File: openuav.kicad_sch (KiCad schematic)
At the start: 35 parts, among them J1 Conn_01x06, J31 Conn_01x09, J32 Conn_01x09, J33 Conn_01x09, J99 USB_C_Receptacle_USB2.0, U1 STM32G431CBUx, U3 LSM6DSR, U4 LPS22HH, U5 TPS54202DDC, U6 W25N01GVZEIG, U7 XC6206P332MR

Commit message: new PCB WIP
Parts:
- removed J1: Conn_01x06, Connector_PinHeader_2.54mm:PinHeader_2x03_P2.54mm_Vertical, symbol Connector_Generic:Conn_01x06
- removed J31, J32, J33: Conn_01x09, Connector_PinHeader_2.54mm:PinHeader_1x09_P2.54mm_Vertical, symbol Connector_Generic:Conn_01x09
- added C14: 1u, Capacitor_SMD:C_0402_1005Metric, symbol Device:C_Small
- added J1, J10, J11, J12, J13, J14, J15, J16, J17, J18, J19, J2, J20, J21, J22, J23, J24, J25, J26, J27, J28, J29, J3, J30, J31, J32, J4, J5, J6, J7, J8, J9: Conn_01x01, TestPoint:TestPoint_THTPad_1.5x1.5mm_Drill0.7mm, symbol Connector_Generic:Conn_01x01
- added R5: 68k, Resistor_SMD:R_0402_1005Metric, symbol Device:R_Small
- added R6: 10k, Resistor_SMD:R_0402_1005Metric, symbol Device:R_Small
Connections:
- net +3V3: now also J29.1 (Pin_1)
- net +5V: now also J10.1 (Pin_1), J14.1 (Pin_1), J18.1 (Pin_1), J2.1 (Pin_1), J6.1 (Pin_1)
- net +BATT: now also R5.1
- net BOOT0: now also J28.1 (Pin_1)
- net GND: now also C14.2, J1.1 (Pin_1), J13.1 (Pin_1), J17.1 (Pin_1), J21.1 (Pin_1), J27.1 (Pin_1), J5.1 (Pin_1), J9.1 (Pin_1), R6.2
- net I2C_CLK: now also U1.31 (PA9), J20.1 (Pin_1); no longer U1.16 (PC4)
- net I2C_SDA: now also U1.30 (PA8), J19.1 (Pin_1); no longer U1.5 (PF0)
- net NRST: now also J31.1 (Pin_1)
- net PWM_1: now also J22.1 (Pin_1)
- net PWM_2: now also J23.1 (Pin_1)
- net PWM_3: now also J24.1 (Pin_1)
- net PWM_4: now also J25.1 (Pin_1)
- net SPI1_CS: now also U1.18 (PB1); no longer U1.19 (PB2)
- net SPI3_CS: now also U1.44 (PB6); no longer U1.47 (PB9)
- net SPI3_MISO: now also U1.42 (PB4); no longer U1.40 (PC11)
- net SWCLK: now also J30.1 (Pin_1)
- net SWDIO: now also J32.1 (Pin_1)
- net UART_1_RX: now also J3.1 (Pin_1)
- net UART_1_TX: now also U1.16 (PC4), J4.1 (Pin_1); no longer U1.31 (PA9)
- net UART_2_RX: now also U1.38 (PA15), J7.1 (Pin_1); no longer U1.42 (PB4)
- net UART_2_TX: now also J8.1 (Pin_1)
- net UART_3_RX: now also U1.40 (PC11), J11.1 (Pin_1); no longer U1.24 (PB11)
- net UART_3_TX: now also U1.47 (PB9), J12.1 (Pin_1); no longer U1.22 (PB10)
- net CURRENT: now reaches U1.6 (PF1)
- net CURRENT: now also J26.1 (Pin_1)
- new net UART_4_RX: J15.1 (Pin_1), U1.22 (PB10)
- new net UART_4_TX: J16.1 (Pin_1), U1.24 (PB11)
- new net VOLTAGE: C14.1, R5.2, R6.1, U1.5 (PF0)
- no-connect marks 12 -> 11
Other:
- moved on the sheet: H1, H2, H3, H4

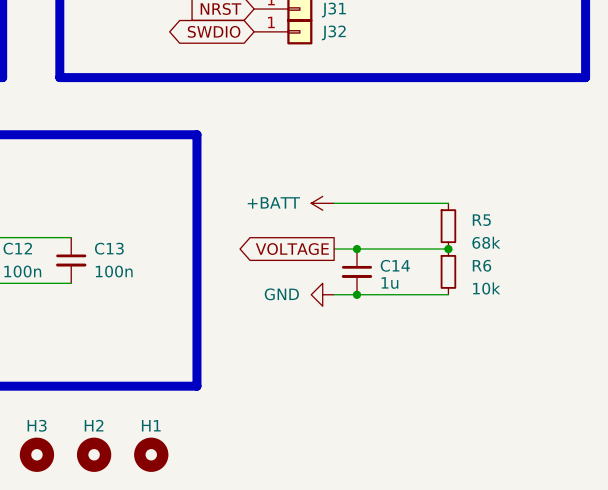
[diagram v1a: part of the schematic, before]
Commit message: Finish draft PCB design
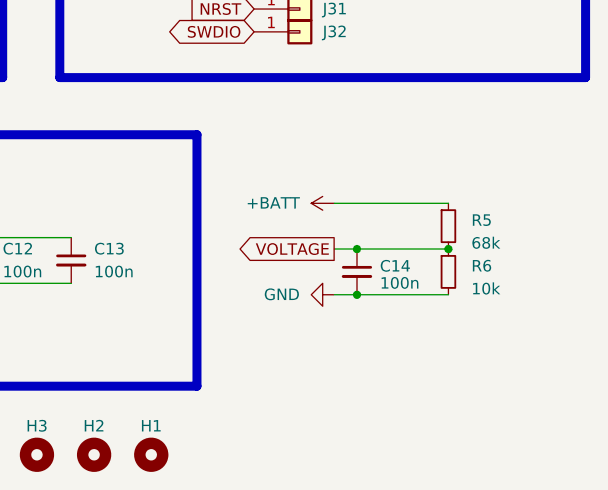
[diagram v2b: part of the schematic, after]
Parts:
- C14: value 1u -> 100n; LCSC (none) -> C307331
- C15: LCSC (none) -> C19702
- J99: footprint Connector_USB:USB_C_Receptacle_GCT_USB4105-xx-A_16P_TopMnt_Horizontal -> Connector_Custom_Pads:TYPE-C-31-M-12; LCSC (none) -> C2894897
- R1, R2: LCSC (none) -> C25905
- R3: LCSC (none) -> C25741
- R4: LCSC (none) -> C852522
- R5: LCSC (none) -> C36871
- R6: LCSC (none) -> C17414
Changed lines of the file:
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@@
+      (effects (font (size 1.27 1.27)) hide)
+    )
+    (property "LCSC" "C17414" (at 266.7 172.72 0)
       (effects (font (size 1.27 1.27)) hide)
     )
@@
       (effects (font (size 1.27 1.27)) hide)
     )
-    (property "LCSC" "" (at 138.43 172.72 0)
+    (property "LCSC" "C19702" (at 138.43 172.72 0)
       (effects (font (size 1.27 1.27)) hide)
     )
@@
       (effects (font (size 1.27 1.27)) hide)
     )
+    (property "LCSC" "C25905" (at 109.22 127 0)
+      (effects (font (size 1.27 1.27)) hide)
+    )
     (pin "1")
     (pin "2")
@@
     )
     (property "Datasheet" "~" (at 115.57 127 0)
+      (effects (font (size 1.27 1.27)) hide)
+    )
+    (property "LCSC" "C25905" (at 115.57 127 0)
       (effects (font (size 1.27 1.27)) hide)
     )
@@
       (effects (font (size 1.27 1.27)) hide)
     )
+    (property "LCSC" "C36871" (at 266.7 167.64 0)
+      (effects (font (size 1.27 1.27)) hide)
+    )
     (pin "1")
     (pin "2")
@@
       (effects (font (size 1.27 1.27)) (justify left))
     )
-    (property "Value" "1u" (at 259.08 173.99 0)
+    (property "Value" "100n" (at 259.08 173.99 0)
       (effects (font (size 1.27 1.27)) (justify left))
     )
@@
     )
     (property "Datasheet" "~" (at 256.54 172.72 0)
+      (effects (font (size 1.27 1.27)) hide)
+    )
+    (property "LCSC" "C307331" (at 256.54 172.72 0)
       (effects (font (size 1.27 1.27)) hide)
     )
@@
       (effects (font (size 1.27 1.27)) (justify right) hide)
     )
-    (property "Footprint" "Connector_USB:USB_C_Receptacle_GCT_USB4105-xx-A_16P_TopMnt_Horizontal" (at 133.35 114.3 0)
+    (property "Footprint" "Connector_Custom_Pads:TYPE-C-31-M-12" (at 133.35 114.3 0)
       (effects (font (size 1.27 1.27)) hide)
     )
     (property "Datasheet" "https://www.usb.org/sites/default/files/documents/usb_type-c.zip" (at 133.35 114.3 0)
+      (effects (font (size 1.27 1.27)) hide)
+    )
+    (property "LCSC" "C2894897" (at 137.16 114.3 0)
       (effects (font (size 1.27 1.27)) hide)
     )
@@
     )
     (property "Datasheet" "~" (at 71.755 175.26 0)
+      (effects (font (size 1.27 1.27)) hide)
+    )
+    (property "LCSC" "C852522" (at 71.755 175.26 0)
       (effects (font (size 1.27 1.27)) hide)
     )
@@
       (effects (font (size 1.27 1.27)) hide)
     )
+    (property "LCSC" "C25741" (at 71.755 170.18 0)
+      (effects (font (size 1.27 1.27)) hide)
+    )

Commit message: tidying
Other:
- note added: "Battery voltage sense"
- note added: "TODO: LED TODO: Buzzer"
- note removed: "TODO: LEDs TODO: Buzzer TODO: ADC voltage sense"
- moved on the sheet: C14, H1, H2, H3, H4, J21, J22, J23, J24, J25, J26, J27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

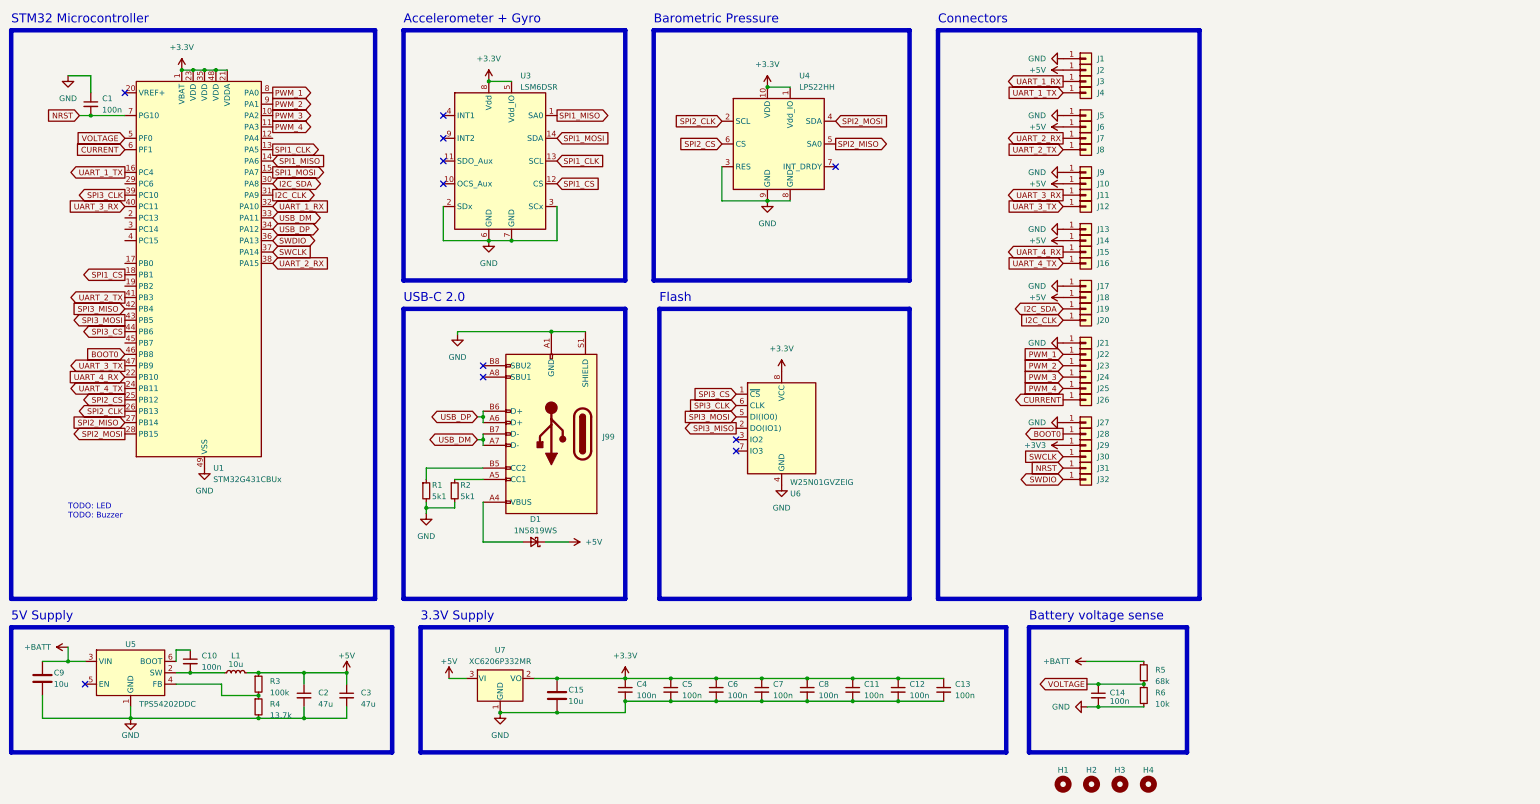
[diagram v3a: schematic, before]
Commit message: Add buzzer connection, minor layout improvements
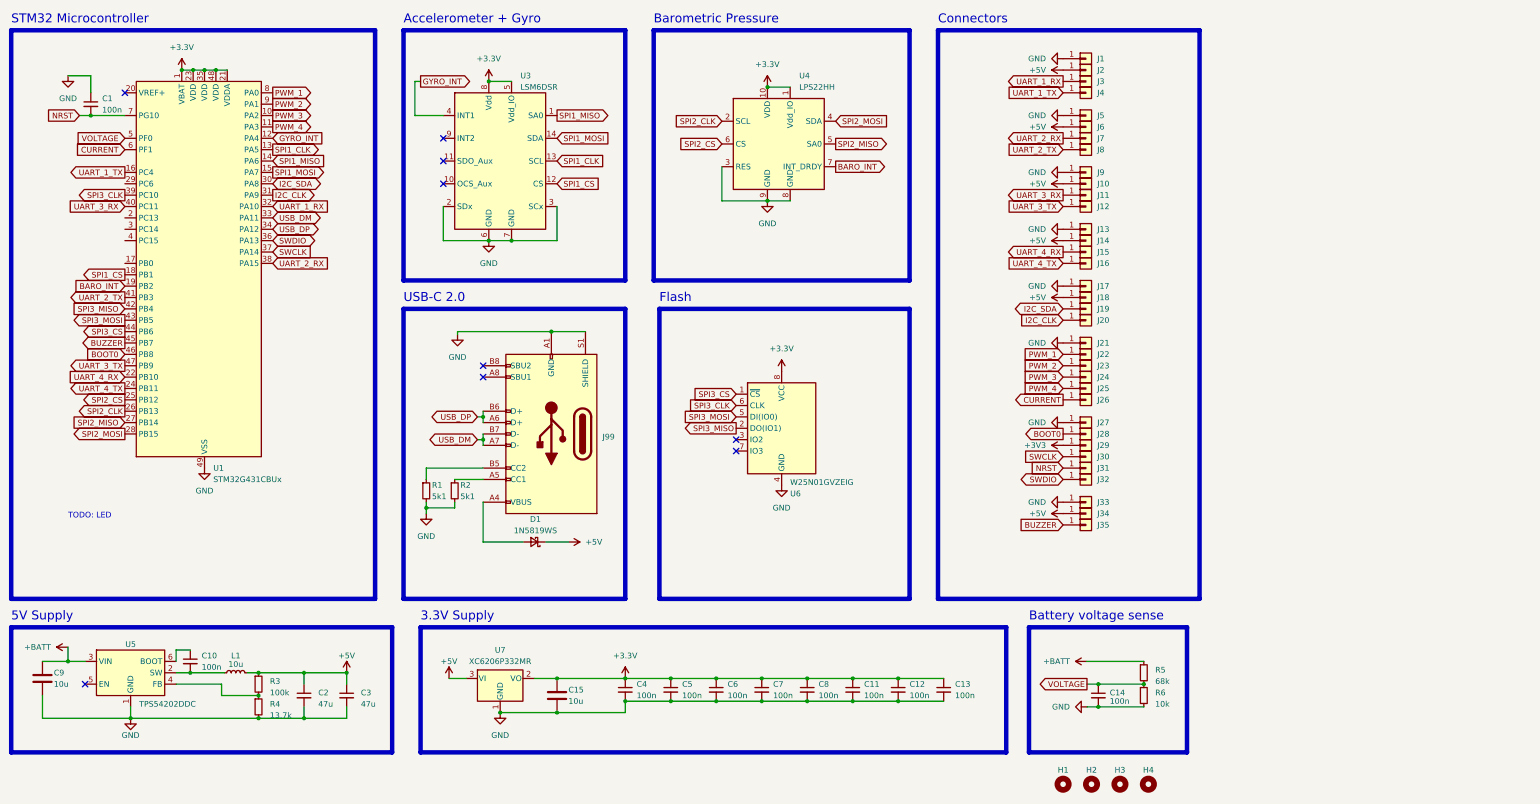
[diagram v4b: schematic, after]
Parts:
- added J33, J34, J35: Conn_01x01, TestPoint:TestPoint_THTPad_1.5x1.5mm_Drill0.7mm, symbol Connector_Generic:Conn_01x01
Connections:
- net +5V: now also J34.1 (Pin_1)
- net GND: now also J33.1 (Pin_1)
- net GYRO_INT: now reaches U3.4 (INT1)
- net GYRO_INT: now also U1.12 (PA4)
- net BARO_INT: now reaches U4.7 (INT_DRDY)
- net BARO_INT: now also U1.19 (PB2)
- net BUZZER: now reaches U1.45 (PB7)
- net BUZZER: now also J35.1 (Pin_1)
- no-connect marks 11 -> 9
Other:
- note added: "TODO: LED"
- note removed: "TODO: LED TODO: Buzzer"
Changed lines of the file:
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@@
   (no_connect (at 121.92 99.06))
   (no_connect (at 113.03 53.34))
-  (no_connect (at 200.66 54.61))
   (no_connect (at 113.03 58.42))
   (no_connect (at 121.92 101.6))
   (no_connect (at 178.435 115.57))
   (no_connect (at 33.02 170.18))
-  (no_connect (at 113.03 43.18))
   (wire (pts (xy 34.29 43.18) (xy 41.91 43.18))
     (stroke (width 0) (type default))
@@
     (stroke (width 0) (type default))
   )
+  (wire (pts (xy 106.68 35.56) (xy 106.68 43.18))
+    (stroke (width 0) (type default))
+  )
   (wire (pts (xy 120.65 110.49) (xy 121.92 110.49))
     (stroke (width 0) (type default))
@@
     (stroke (width 0) (type default))
   )
+  (wire (pts (xy 107.95 35.56) (xy 106.68 35.56))
+    (stroke (width 0) (type default))
+  )
   (wire (pts (xy 125.73 176.53) (xy 138.43 176.53))
     (stroke (width 0) (type default))
@@
   )
   (wire (pts (xy 184.15 173.99) (xy 194.31 173.99))
+    (stroke (width 0) (type default))
+  )
+  (wire (pts (xy 106.68 43.18) (xy 113.03 43.18))
     (stroke (width 0) (type default))
   )
@@
     (effects (font (size 2 2)) (justify left bottom))
   )
-  (text "TODO: LED\nTODO: Buzzer" (at 29.21 133.35 0)
+  (text "TODO: LED" (at 29.21 133.35 0)
     (effects (font (size 1.27 1.27)) (justify left bottom))
   )
@@
     )
   )
+  (global_label "BUZZER" (shape input) (at 251.46 134.62 180) (fields_autoplaced)
+    (effects (font (size 1.27 1.27)) (justify right))
+    (property "Intersheetrefs" "${INTERSHEET_REFS}" (at 241.1157 134.62 0)
+      (effects (font (size 1.27 1.27)) (justify right) hide)
+    )
+  )
   (global_label "SPI2_MISO" (shape output) (at 200.66 49.53 0) (fields_autoplaced)
     (effects (font (size 1.27 1.27)) (justify left))
@@
     )
   )
+  (global_label "BUZZER" (shape output) (at 41.91 93.98 180) (fields_autoplaced)
+    (effects (font (size 1.27 1.27)) (justify right))
+    (property "Intersheetrefs" "${INTERSHEET_REFS}" (at 31.5657 93.98 0)
+      (effects (font (size 1.27 1.27)) (justify right) hide)
+    )
+  )
   (global_label "PWM_4" (shape input) (at 251.46 104.14 180) (fields_autoplaced)
     (effects (font (size 1.27 1.27)) (justify right))
@@
     )
   )
+  (global_label "GYRO_INT" (shape output) (at 107.95 35.56 0) (fields_autoplaced)
+    (effects (font (size 1.27 1.27)) (justify left))
+    (property "Intersheetrefs" "${INTERSHEET_REFS}" (at 119.6854 35.56 0)
+      (effects (font (size 1.27 1.27)) (justify left) hide)
+    )
+  )
   (global_label "UART_2_RX" (shape input) (at 74.93 76.2 0) (fields_autoplaced)
     (effects (font (size 1.27 1.27)) (justify left))
@@
     )
   )
+  (global_label "BARO_INT" (shape output) (at 200.66 54.61 0) (fields_autoplaced)
+    (effects (font (size 1.27 1.27)) (justify left))
+    (property "Intersheetrefs" "${INTERSHEET_REFS}" (at 212.3954 54.61 0)
+      (effects (font (size 1.27 1.27)) (justify left) hide)
+    )
+  )
   (global_label "SPI1_MOSI" (shape input) (at 138.43 48.26 0) (fields_autoplaced)
     (effects (font (size 1.27 1.27)) (justify left))
@@
     )
   )
+  (global_label "GYRO_INT" (shape input) (at 74.93 48.26 0) (fields_autoplaced)
+    (effects (font (size 1.27 1.27)) (justify left))
+    (property "Intersheetrefs" "${INTERSHEET_REFS}" (at 86.6654 48.26 0)
+      (effects (font (size 1.27 1.27)) (justify left) hide)
+    )
+  )
   (global_label "VOLTAGE" (shape input) (at 41.91 48.26 180) (fields_autoplaced)
     (effects (font (size 1.27 1.27)) (justify right))
@@
     )
   )
+  (global_label "BARO_INT" (shape input) (at 41.91 81.28 180) (fields_autoplaced)
+    (effects (font (size 1.27 1.27)) (justify right))
+    (property "Intersheetrefs" "${INTERSHEET_REFS}" (at 30.1746 81.28 0)
+      (effects (font (size 1.27 1.27)) (justify right) hide)
+    )
+  )
   (global_label "UART_4_RX" (shape output) (at 251.46 73.66 180) (fields_autoplaced)
     (effects (font (size 1.27 1.27)) (justify right))
@@
         (path "/e63e39d7-6ac0-4ffd-8aa3-1841a4541b55"
           (reference "H1") (unit 1)
+        )
+      )
+    )
+  )
+  (symbol (lib_id "power:+5V") (at 251.46 132.08 90) (unit 1)
+    (in_bom yes) (on_board yes) (dnp no)
+    (property "Reference" "#PWR022" (at 255.27 132.08 0)
+      (effects (font (size 1.27 1.27)) hide)
+    )
+    (property "Value" "+5V" (at 247.65 132.08 90)
+      (effects (font (size 1.27 1.27)) (justify left))
+    )
+    (property "Footprint" "" (at 251.46 132.08 0)
+      (effects (font (size 1.27 1.27)) hide)
+    )
+    (property "Datasheet" "" (at 251.46 132.08 0)
+      (effects (font (size 1.27 1.27)) hide)
+    )
+    (pin "1")
+    (instances
+      (project "openuav"
+        (path "/e63e39d7-6ac0-4ffd-8aa3-1841a4541b55"
+          (reference "#PWR022") (unit 1)
         )
       )
@@
     )
   )
+  (symbol (lib_id "Connector_Generic:Conn_01x01") (at 256.54 129.54 0) (unit 1)
+    (in_bom yes) (on_board yes) (dnp no)
+    (property "Reference" "J33" (at 259.08 129.54 0)
+      (effects (font (size 1.27 1.27)) (justify left))
+    )
+    (property "Value" "Conn_01x01" (at 259.08 131.445 0)
+      (effects (font (size 1.27 1.27)) (justify left) hide)
+    )
+    (property "Footprint" "TestPoint:TestPoint_THTPad_1.5x1.5mm_Drill0.7mm" (at 256.54 129.54 0)
+      (effects (font (size 1.27 1.27)) hide)
+    )
+    (property "Datasheet" "~" (at 256.54 129.54 0)
+      (effects (font (size 1.27 1.27)) hide)
+    )
+    (pin "1")
+    (instances
+      (project "openuav"
+        (path "/e63e39d7-6ac0-4ffd-8aa3-1841a4541b55"
+          (reference "J33") (unit 1)
+        )
+      )
+    )
+  )
   (symbol (lib_id "Connector_Generic:Conn_01x01") (at 256.54 111.76 0) (unit 1)
     (in_bom yes) (on_board yes) (dnp no)
@@
     )
   )
+  (symbol (lib_id "Connector_Generic:Conn_01x01") (at 256.54 134.62 0) (unit 1)
+    (in_bom yes) (on_board yes) (dnp no)
+    (property "Reference" "J35" (at 259.08 134.62 0)
+      (effects (font (size 1.27 1.27)) (justify left))
+    )
+    (property "Value" "Conn_01x01" (at 259.08 136.525 0)
+      (effects (font (size 1.27 1.27)) (justify left) hide)
+    )
+    (property "Footprint" "TestPoint:TestPoint_THTPad_1.5x1.5mm_Drill0.7mm" (at 256.54 134.62 0)
+      (effects (font (size 1.27 1.27)) hide)
+    )
+    (property "Datasheet" "~" (at 256.54 134.62 0)
+      (effects (font (size 1.27 1.27)) hide)
+    )
+    (pin "1")
+    (instances
+      (project "openuav"
+        (path "/e63e39d7-6ac0-4ffd-8aa3-1841a4541b55"
+          (reference "J35") (unit 1)
+        )
+      )
+    )
+  )
   (symbol (lib_id "Connector_Generic:Conn_01x01") (at 256.54 121.92 0) (unit 1)
     (in_bom yes) (on_board yes) (dnp no)
@@
         (path "/e63e39d7-6ac0-4ffd-8aa3-1841a4541b55"
           (reference "J16") (unit 1)
+        )
+      )
+    )
+  )
+  (symbol (lib_name "GND_1") (lib_id "power:GND") (at 251.46 129.54 270) (unit 1)
+    (in_bom yes) (on_board yes) (dnp no)
+    (property "Reference" "#PWR021" (at 245.11 129.54 0)
+      (effects (font (size 1.27 1.27)) hide)
+    )
+    (property "Value" "GND" (at 247.65 129.54 90)
+      (effects (font (size 1.27 1.27)) (justify right))
+    )
+    (property "Footprint" "" (at 251.46 129.54 0)
+      (effects (font (size 1.27 1.27)) hide)
+    )
+    (property "Datasheet" "" (at 251.46 129.54 0)
+      (effects (font (size 1.27 1.27)) hide)
+    )
+    (pin "1")
+    (instances
+      (project "openuav"
+        (path "/e63e39d7-6ac0-4ffd-8aa3-1841a4541b55"
+          (reference "#PWR021") (unit 1)
         )
       )
@@
         )
       )
+    )
+  )
+  (symbol (lib_id "Connector_Generic:Conn_01x01") (at 256.54 132.08 0) (unit 1)
+    (in_bom yes) (on_board yes) (dnp no)
+    (property "Reference" "J34" (at 259.08 132.08 0)
+      (effects (font (size 1.27 1.27)) (justify left))
+    )
+    (property "Value" "Conn_01x01" (at 259.08 133.985 0)
+      (effects (font (size 1.27 1.27)) (justify left) hide)
+    )
+    (property "Footprint" "TestPoint:TestPoint_THTPad_1.5x1.5mm_Drill0.7mm" (at 256.54 132.08 0)
+      (effects (font (size 1.27 1.27)) hide)
+    )
+    (property "Datasheet" "~" (at 256.54 132.08 0)
+      (effects (font (size 1.27 1.27)) hide)
+    )
+    (pin "1")
+    (instances
+      (project "openuav"
+        (path "/e63e39d7-6ac0-4ffd-8aa3-1841a4541b55"
+          (reference "J34") (unit 1)
+        )
+      )
